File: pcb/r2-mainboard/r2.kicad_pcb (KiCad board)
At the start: 4 copper layers, 185.5 x 95 mm, 327 parts, among them J1 USB-C 16P, J2 Pico-Lock 504050-0391, J20 SWD+JTAG (DNP), J21 MICRO_SD(TFC-WPAPR-08), J22 HC-FPC-05-09-6RLTAG, J23 HC-FPC-05-09-6RLTAG, J24 HC-FPC-05-09-8RLTAG, J25 SolderPads 3x, J26 BTH-060-01-L-D-A-K-TR, J27 BTH-060-01-L-D-A-K-TR, J6 FPC-05F-50PH20, Q1 AO3401A, Q2 S8050, Q6 AO3400A, Q7 AO3401A, Q8 AO3401A, Q9 AO3400A, SW20 SW, SW21 SW, SW22 SW, U1 BQ25892RTW, U10 TPS7A0233DBVR, U12 TPS61022RWUR, U13 TPS63802DLAR, U14 TPS62A02DRLR, U15 TPS62A02DRLR, U2 MAX17048G+T10, U20 STM32G0B1RCT6, U21 INA3221, U22 INA3221, U23 LGS6302B5, U24 LGS6302B5, U26 LGS5145, U27 INA3221, U3 USBLC6-2SC6, U31 LM321, U41 XC6SLX-FTG256, U42 W25Q128JVSIQ, U52 MT41K64M16TW, U53 LM3630A, U54 TPS22914BYFPR, U55 TPS22914BYFPR, U6 MT9700, U7 TPS22914BYFPR, U8 TPS22914BYFPR, U9 LGS5145, X1 33.33MHz, X2 PCM-071, Y20 32.768kHz

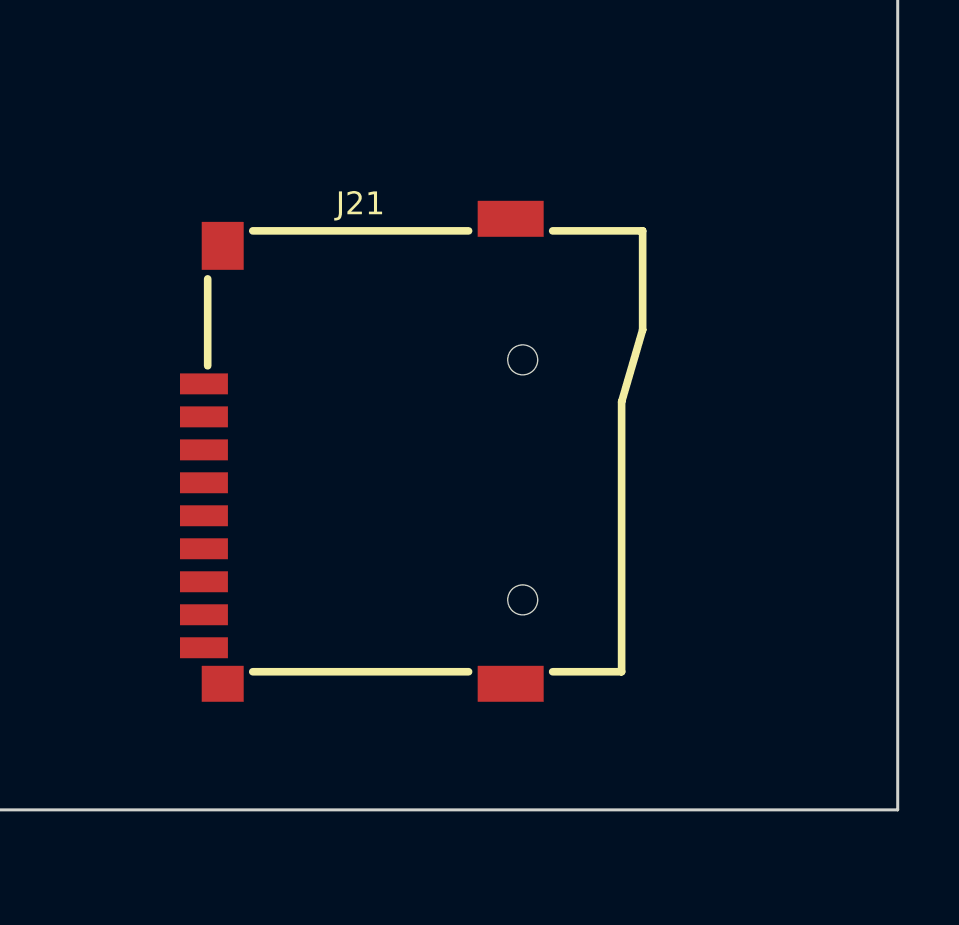
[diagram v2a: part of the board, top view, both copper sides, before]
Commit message: R2: 3D models — 322 of 327 now resolve, and the other five say why
After the path fix set KICAD10_3DMODEL_DIR, 311 of 327 footprints already
resolved. tools/add_3d_models.py handles the rest and makes the project
self-contained: everything it uses lands in 3dmodels/ referenced by
${KIPRJMOD}, so the 3D view works on any clone.

The assumption that R1 has these models is half right in a way worth
recording. pcb_common keeps 66 STEP files NEXT TO its footprints rather than
in a .3dshapes directory, which is why searching for 3D directories finds
nothing -- but several are referenced by absolute paths from the original
author, J24's pointing at /Users/wenting/Documents/projects/Enchanter/... .
Those are real models and are now copied in and re-pointed: J1's actual
HRO TYPE-C-31-M-12 (whose filename in pcb_common has a double space), J24,
J21's microSD socket and J6's panel connector. R1's own board is no better
off: 349 of its 378 model references point at files that do not exist.

The Spartan-6 is the other case entirely. footprints:Xilinx_FTG256 is a
pcb_common custom footprint whose model lived on the Modos author's KiCad 6
install -- hence ${KICAD6_3DMODEL_DIR}, a variable nothing defines any more
-- and KiCad's library has no Xilinx_FTG256 either. It now uses
BGA-256_17.0x17.0mm_Layout16x16_P1.0mm, which is the FTG256's exact
geometry. Six other parts get dimensional stand-ins, each recorded with what
matches and what does not.

Five are left with nothing, deliberately rather than faked: X1, L1, J2, U53
and J25 (which is bare copper pads and correctly has none). J2 is the one to
resist substituting -- only a 1.25 mm PicoBlade model exists, a different
connector, and it sits at the board edge where a wrong body would mislead
the enclosure check.

⚠ A stand-in is for clearance and collision, not identity. Body and height
are right; pin detail and markings are not.

One KiCad behaviour worth knowing: a footprint edited in the library does
not propagate to a board tha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
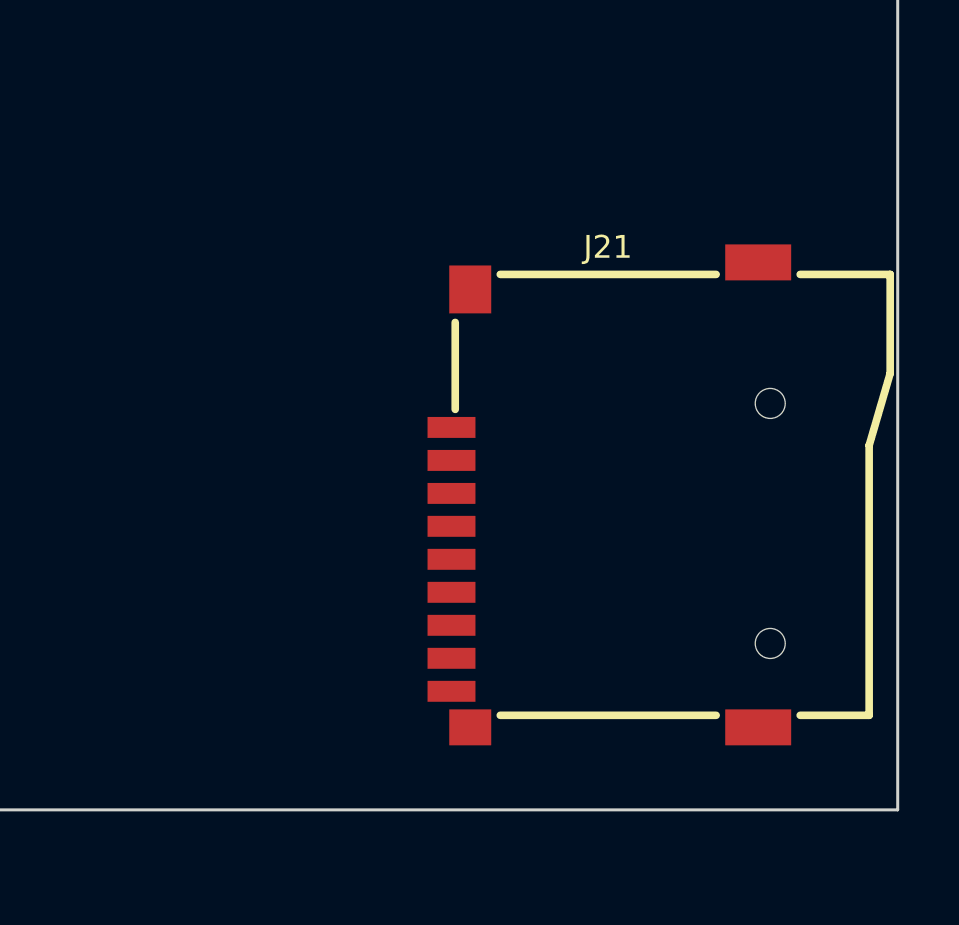
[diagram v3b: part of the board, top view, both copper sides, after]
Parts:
- moved J21 8.38 mm to (265.0, 103.0)
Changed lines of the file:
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@@
 		)
 		(embedded_fonts no)
+		(model "${KIPRJMOD}/3dmodels/BTH-060-01-L-D-A-K-TR.stp"
+			(offset (xyz 0 0 0))
+			(scale (xyz 1 1 1))
+			(rotate (xyz 0 0 0))
+		)
 	)
 	(footprint "Resistor_SMD:R_0402_1005Metric"
@@
 		)
 		(embedded_fonts no)
-		(model "${KICAD10_3DMODEL_DIR}/Connector_USB.3dshapes/USB_C_Receptacle_HRO_TYPE-C-31-M-12.step"
-			(offset
-				(xyz 0 0 0)
-			)
-			(scale
-				(xyz 1 1 1)
-			)
-			(rotate
-				(xyz 0 0 0)
-			)
+		(model "${KIPRJMOD}/3dmodels/HRO_TYPE-C-31-M-12.step"
+			(offset (xyz 0 0 0))
+			(scale (xyz 1 1 1))
+			(rotate (xyz 0 0 0))
 		)
 	)
@@
 		)
 		(embedded_fonts no)
-		(model "/Users/wenting/Documents/projects/Enchanter/pcb/pcb_common/footprints.pretty/FPC-SMD_8P-P0.50_HC-FPC-05-09-8RLTAG.step"
-			(offset
-				(xyz 0 0.65 0)
-			)
-			(scale
-				(xyz 1 1 1)
-			)
-			(rotate
-				(xyz 0 0 -180)
-			)
+		(model "${KIPRJMOD}/3dmodels/FPC-SMD_8P-P0.50_HC-FPC-05-09-8RLTAG.step"
+			(offset (xyz 0 0 0))
+			(scale (xyz 1 1 1))
+			(rotate (xyz 0 0 0))
 		)
 	)
 	(footprint "r2:PCM-071_Module"
 		(layer "F.Cu")
-		(attr exclude_from_pos_files allow_missing_courtyard)
 		(at 164.2 41.028 90)
 		(descr "PHYTEC phyCORE-AM62x PCM-071, module outline and M2.5 mounting holes. NO PADS -- the 240 contacts belong to J26/J27, the two BTH-060 receptacles. The module is fitted by hand after assembly, so this is excluded from the position file. Outline and hole positions from PCM-071_1573-1.dxf (BOARD_OUTLINE 32.000 x 43.000; holes at 2.800/2.800 and 29.200/40.200, 2.600 drill, 4.000 plating). Stands 5 mm off the board on two M2.5 F-F standoffs. See som.md section 11.")
@@
 			)
 		)
+		(attr exclude_from_pos_files allow_missing_courtyard)
 		(duplicate_pad_numbers_are_jumpers no)
 		(fp_line
@@
 		)
 		(fp_rect
-			(start -16 21.5)
-			(end 16 -21.5)
+			(start -14.1845 -19.9)
+			(end -8.2155 15.1)
 			(stroke
 				(width 0.1)
@@
 			)
 			(fill no)
-			(layer "F.Fab")
+			(layer "Dwgs.User")
 		)
-		(fp_circle
-			(center 13.2 -18.7)
-			(end 15.2 -18.7)
+		(fp_rect
+			(start 8.2155 -15.1)
+			(end 14.1845 19.9)
 			(stroke
 				(width 0.1)
-				(type dash)
+				(type solid)
 			)
 			(fill no)
-			(layer "F.Fab")
+			(layer "Dwgs.User")
 		)
-		(fp_circle
-			(center -13.2 18.7)
-			(end -11.2 18.7)
+		(fp_rect
+			(start -16 21.5)
+			(end 16 -21.5)
 			(stroke
 				(width 0.1)
-				(type dash)
+				(type solid)
 			)
 			(fill no)
-			(layer "F.Fab")
+			(layer "Dwgs.User")
 		)
 		(fp_rect
-			(start -14.1845 -19.9)
-			(end -8.2155 15.1)
+			(start -16 21.5)
+			(end 16 -21.5)
 			(stroke
 				(width 0.1)
@@
 			)
 			(fill no)
-			(layer "Dwgs.User")
+			(layer "F.Fab")
 		)
-		(fp_rect
-			(start 8.2155 -15.1)
-			(end 14.1845 19.9)
+		(fp_circle
+			(center 13.2 -18.7)
+			(end 15.2 -18.7)
 			(stroke
 				(width 0.1)
-				(type solid)
+				(type dash)
 			)
 			(fill no)
-			(layer "Dwgs.User")
+			(layer "F.Fab")
 		)
-		(fp_rect
-			(start -16 21.5)
-			(end 16 -21.5)
+		(fp_circle
+			(center -13.2 18.7)
+			(end -11.2 18.7)
 			(stroke
 				(width 0.1)
-				(type solid)
+				(type dash)
 			)
 			(fill no)
-			(layer "Dwgs.User")
+			(layer "F.Fab")
 		)
 		(pad "" np_thru_hole circle
@@
 		)
 		(embedded_fonts no)
+		(model "${KIPRJMOD}/3dmodels/PCM-071.step"
+			(offset (xyz 0 0 0))
+			(scale (xyz 1 1 1))
+			(rotate (xyz 0 0 0))
+		)
 	)
 	(footprint "Resistor_SMD:R_0402_1005Metric"
@@
 		)
 		(embedded_fonts no)
+		(model "${KICAD10_3DMODEL_DIR}/Package_DFN_QFN.3dshapes/DFN-10-1EP_2x3mm_P0.5mm_EP0.64x2.4mm.step"
+			(offset (xyz 0 0 0))
+			(scale (xyz 1 1 1))
+			(rotate (xyz 0 0 0))
+		)
 	)
 	(footprint "Resistor_SMD:R_0402_1005Metric"
@@
 		)
 		(embedded_fonts no)
-		(model "${KICAD10_3DMODEL_DIR}/Package_DFN_QFN.3dshapes/Texas_RGV0016A_VQFN-16-1EP_4x4mm_P0.65mm_EP2.1x2.1mm.step"
-			(offset
-				(xyz 0 0 0)
-			)
-			(scale
-				(xyz 1 1 1)
-			)
-			(rotate
-				(xyz 0 0 0)
-			)
+		(model "${KICAD10_3DMODEL_DIR}/Package_DFN_QFN.3dshapes/Texas_RSA_VQFN-16-1EP_4x4mm_P0.65mm_EP2.7x2.7mm.step"
+			(offset (xyz 0 0 0))
+			(scale (xyz 1 1 1))
+			(rotate (xyz 0 0 0))
 		)
 	)
@@
 		)
 		(embedded_fonts no)
-		(model "${KICAD10_3DMODEL_DIR}/Package_DFN_QFN.3dshapes/Texas_RWU0007A_VQFN-7_2x2mm_P0.5mm.step"
-			(offset
-				(xyz 0 0 0)
-			)
-			(scale
-				(xyz 1 1 1)
-			)
-			(rotate
-				(xyz 0 0 0)
-			)
+		(model "${KICAD10_3DMODEL_DIR}/Package_DFN_QFN.3dshapes/DFN-8-1EP_2x2mm_P0.5mm_EP0.6x1.2mm.step"
+			(offset (xyz 0 0 0))
+			(scale (xyz 1 1 1))
+			(rotate (xyz 0 0 0))
 		)
 	)
@@
 		)
 		(embedded_fonts no)
-		(model "${KICAD10_3DMODEL_DIR}/Package_DFN_QFN.3dshapes/Texas_RGV0016A_VQFN-16-1EP_4x4mm_P0.65mm_EP2.1x2.1mm.step"
-			(offset
-				(xyz 0 0 0)
-			)
-			(scale
-				(xyz 1 1 1)
-			)
-			(rotate
-				(xyz 0 0 0)
-			)
+		(model "${KICAD10_3DMODEL_DIR}/Package_DFN_QFN.3dshapes/Texas_RSA_VQFN-16-1EP_4x4mm_P0.65mm_EP2.7x2.7mm.step"
+			(offset (xyz 0 0 0))
+			(scale (xyz 1 1 1))
+			(rotate (xyz 0 0 0))
 		)
 	)
@@
 		)
 		(embedded_fonts no)
-		(model "${KIPRJMOD}/datasheets/SoM Phycore AM62x/BTH-060-01-L-D-A-K-TR/BTH-060-01-L-D-A-K-TR.stp"
-			(offset
-				(xyz 0 0 0)
-			)
-			(scale
-				(xyz 1 1 1)
-			)
-			(rotate
-				(xyz -90 -0 -90)
-			)
+		(model "${KIPRJMOD}/3dmodels/BTH-060-01-L-D-A-K-TR.stp"
+			(offset (xyz 0 0 0))
+			(scale (xyz 1 1 1))
+			(rotate (xyz 0 0 0))
 		)
 	)
@@
 		(model "${KICAD10_3DMODEL_DIR}/Connector_FFC-FPC.3dshapes/Hirose_FH12-8S-0.5SH_1x08-1MP_P0.50mm_Horizontal.step"
 			(offset
-				(xyz 0 0 0)
+				(xyz 0 -0.8 0)
 			)
 			(scale
-				(xyz 1 1 1)
+				(xyz 0.8 0.8 0.8)
 			)
 			(rotate
-				(xyz 0 0 0)
+				(xyz -0 -0 -90)
 			)
 		)
@@
 		)
 		(embedded_fonts no)
-		(model "${KICAD10_3DMODEL_DIR}/Package_DFN_QFN.3dshapes/Texas_RGV0016A_VQFN-16-1EP_4x4mm_P0.65mm_EP2.1x2.1mm.step"
-			(offset
-				(xyz 0 0 0)
-			)
-			(scale
-				(xyz 1 1 1)
-			)
-			(rotate
-				(xyz 0 0 0)
-			)
+		(model "${KICAD10_3DMODEL_DIR}/Package_DFN_QFN.3dshapes/Texas_RSA_VQFN-16-1EP_4x4mm_P0.65mm_EP2.7x2.7mm.step"
+			(offset (xyz 0 0 0))
+			(scale (xyz 1 1 1))
+			(rotate (xyz 0 0 0))
 		)
 	)
@@
 		)
 		(embedded_fonts no)
-		(model "${KIPRJMOD}/../pcb_common/footprints.pretty/FPC-SMD_50P-P0.50_FPC-05F-50PH20.step"
-			(offset
-				(xyz 0 1.6 0)
-			)
-			(scale
-				(xyz 1 1 1)
-			)
-			(rotate
-				(xyz 0 0 0)
-			)
+		(model "${KIPRJMOD}/3dmodels/FPC-SMD_50P-P0.50_FPC-05F-50PH20.step"
+			(offset (xyz 0 0 0))
+			(scale (xyz 1 1 1))
+			(rotate (xyz 0 0 0))
 		)
 	)
@@
 	(footprint "footprints:TFC-WPAPR-08"
 		(layer "F.Cu")
-		(at 256.7488 101.548)
+		(at 265 103)
 		(descr "OFFSET X-> -0.950MM")
 		(tags "OFFSET X-> -0.950MM")
@@
 		)
 		(embedded_fonts no)
-		(model "${KIPRJMOD}/../pcb_common/footprints.pretty/HY-TF1007B.STEP"
-			(offset
-				(xyz -7.25 -7.35 0)
-			)
-			(scale
-				(xyz 1 1 1)
-			)
-			(rotate
-				(xyz -90 0 -90)
-			)
+		(model "${KIPRJMOD}/3dmodels/HY-TF1007B.STEP"
+			(offset (xyz 0 0 0))
+			(scale (xyz 1 1 1))
+			(rotate (xyz 0 0 0))
 		)
 	)
@@
 		)
 		(embedded_fonts no)
-		(model "${KICAD10_3DMODEL_DIR}/Button_Switch_SMD.3dshapes/SW_Push_1P1T_XKB_TS-1187A.step"
-			(offset
-				(xyz 0 0 0)
-			)
-			(scale
-				(xyz 1 1 1)
-			)
-			(rotate
-				(xyz 0 0 0)
-			)
+		(model "${KICAD10_3DMODEL_DIR}/Button_Switch_SMD.3dshapes/SW_Push_1P1T_NO_CK_KMR2.step"
+			(offset (xyz 0 0 0))
+			(scale (xyz 1 1 1))
+			(rotate (xyz 0 0 0))
 		)
 	)
@@
 		)
 		(embedded_fonts no)
-		(model "${KICAD6_3DMODEL_DIR}/Package_BGA.3dshapes/Xilinx_FTG256.wrl"
-			(offset
-				(xyz 0 0 0)
-			)
-			(scale
-				(xyz 1 1 1)
-			)
-			(rotate
-				(xyz 0 0 0)
-			)
+		(model "${KICAD10_3DMODEL_DIR}/Package_BGA.3dshapes/BGA-256_17.0x17.0mm_Layout16x16_P1.0mm_Ball0.5mm_Pad0.4mm_NSMD.step"
+			(offset (xyz 0 0 0))
+			(scale (xyz 1 1 1))
+			(rotate (xyz 0 0 0))
 		)
 	)
@@
 		)
 		(embedded_fonts no)
-		(model "${KICAD10_3DMODEL_DIR}/Package_DFN_QFN.3dshapes/WQFN-24-1EP_4x4mm_P0.5mm_EP2.6x2.6mm.step"
-			(offset
-				(xyz 0 0 0)
-			)
-			(scale
-				(xyz 1 1 1)
-			)
-			(rotate
-				(xyz 0 0 0)
-			)
+		(model "${KICAD10_3DMODEL_DIR}/Package_DFN_QFN.3dshapes/Texas_RTW_WQFN-24-1EP_4x4mm_P0.5mm_EP2.7x2.7mm.step"
+			(offset (xyz 0 0 0))
+			(scale (xyz 1 1 1))
+			(rotate (xyz 0 0 0))
 		)
 	)
@@
 		)
 		(embedded_fonts no)
-		(model "${KICAD10_3DMODEL_DIR}/Package_DFN_QFN.3dshapes/TDFN-8-1EP_2x2mm_P0.5mm_EP0.8x1.2mm.step"
-			(offset
-				(xyz 0 0 0)
-			)
-			(scale
-				(xyz 1 1 1)
-			)
-			(rotate
-				(xyz 0 0 0)
-			)
+		(model "${KICAD10_3DMODEL_DIR}/Package_DFN_QFN.3dshapes/DFN-8-1EP_2x2mm_P0.5mm_EP0.6x1.2mm.step"
+			(offset (xyz 0 0 0))
+			(scale (xyz 1 1 1))
+			(rotate (xyz 0 0 0))
 		)
 	)
@@
 		(layer "Edge.Cuts")
 	)
-	(embedded_fonts no)
 	(group "SoM: X2 + J26 + J27"
-		(members
-			"2200e001-a954-48b2-9629-bd47b75f0930"
+		(members "1b24aa06-b18f-4e78-a7c5-cd93cf5dd40f" "2200e001-a954-48b2-9629-bd47b75f0930"
 			"81925fca-ef22-4cca-a487-e84efd632f81"
-			"1b24aa06-b18f-4e78-a7c5-cd93cf5dd40f"
 		)
 	)
+	(embedded_fonts no)
 )

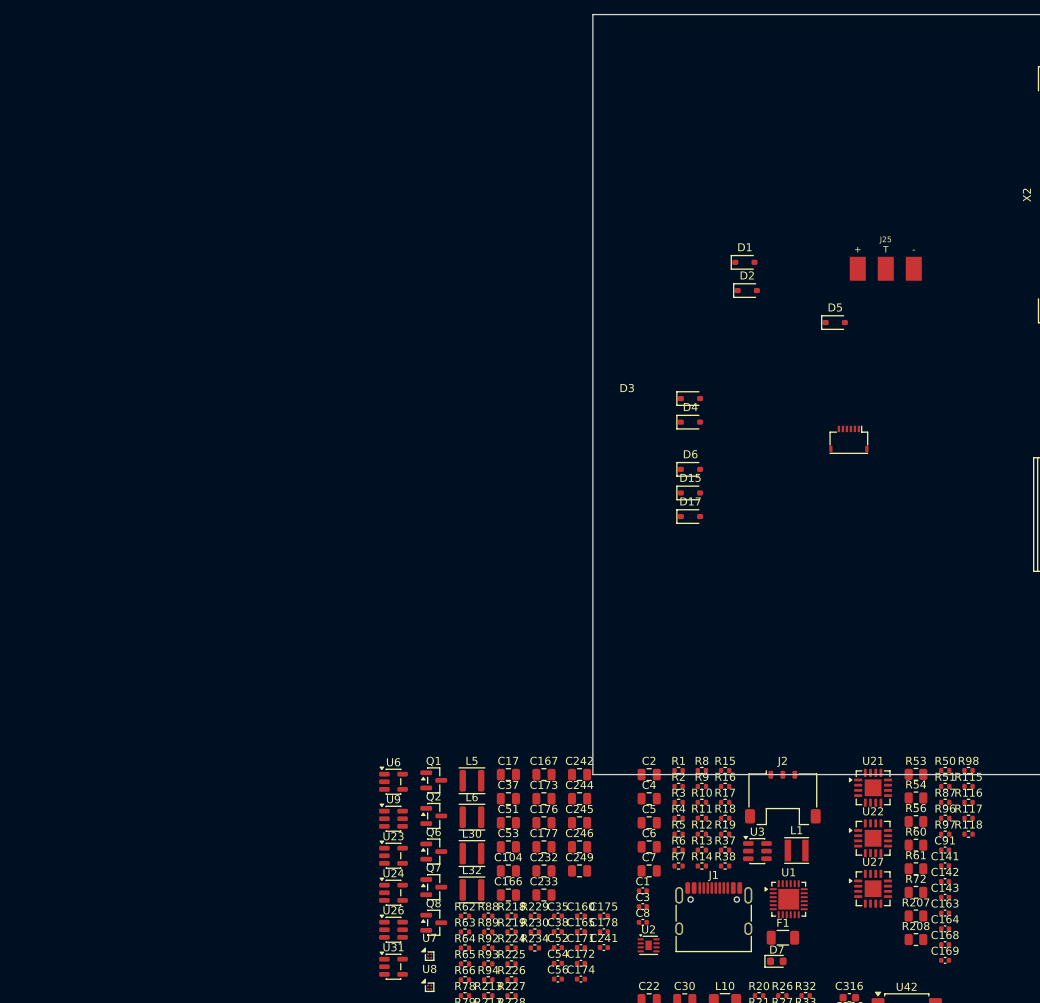
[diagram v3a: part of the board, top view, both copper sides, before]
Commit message: R2: import R1's design settings, and nine net classes with reasons attached
The owner is starting to route and asked what track widths to use. R2's
project file had never been through Board Setup: KiCad 10 stock values (0.4 mm
tracks, 1.651 mm vias) and one stray `power` class whose five patterns match
nets that do not exist on this board.

R2's stackup turns out to be byte-identical to R1's -- same 0.127 mm prepreg,
0.6 mm core, 0.035 mm outer copper, ENIG -- so every geometry R1 proved at
DDR3-666 on a Spartan-6 transfers with its impedance intact. That is the whole
justification for copying rather than calculating, and it is why R1's
SDRAM/EPD/USB widths come across verbatim.

tools/import_r1_settings.py does it in one gated step. It reads R1 read-only,
refuses to write while KiCad is open (KiCad rewrites the project from memory on
save, so the edit would vanish with no error), backs up, and prints every
change plus the reason for each class.

Three things are deliberately not R1's:

- Clearance. layout.md §6.1 used to say start at 0.2 mm. Measuring the placed
  footprints shows that is unusable: KiCad checks class clearance pad-to-pad
  INSIDE a footprint, and U1's BQ25792 has 0.125 mm between pads 1 and 24 --
  0.2 mm would flag eight packages on the day of import. R1's 0.11 mm clears
  every one. §6.1 corrected, the measurements recorded in a new §4.2.

- HV clearance is 0.11 like everything else, and the real separation lives in a
  new r2.kicad_dru rule restricted to tracks. +VGH lands on a 0.5 mm-pitch
  VSON-HR-10 whose own pads sit 0.25 mm apart, so a wide class clearance would
  produce DRC errors no routing can clear.

- An eighth class, EPD, for the 23 EPDC_* nets. layout.md §4's table listed
  seven and was silent on them -- the second-largest routed group on the board.
  R1 had a class for them; without it they would have routed on Default.

check_pcb.py's net-class check was reading the wrong file: it grepped
r2.kicad_pcb for `(net_class "..."` and 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
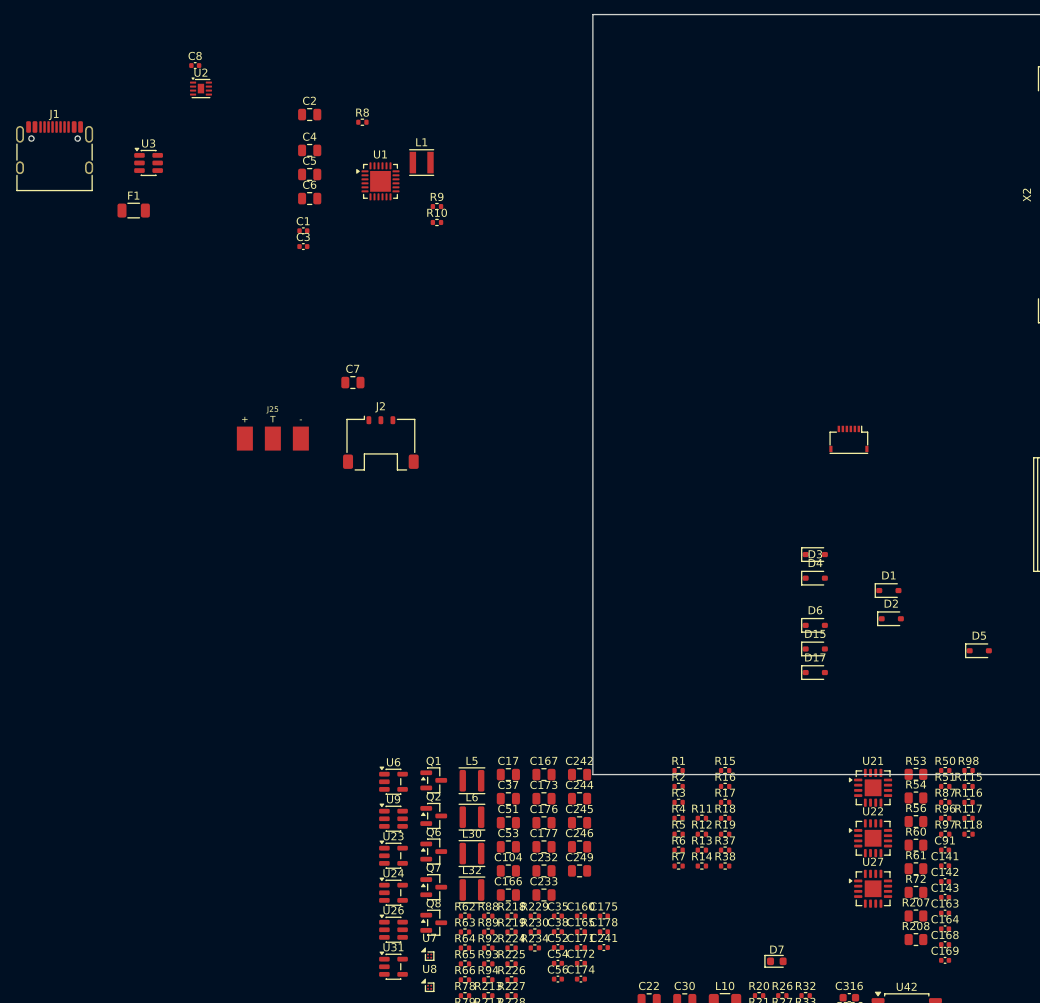
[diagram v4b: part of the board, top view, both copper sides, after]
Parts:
- moved J1 125.8 mm to (19.7, 36.6)
- moved F1 121.9 mm to (29.6, 43.0)
- moved C8 120.8 mm to (37.3, 24.9)
- moved U2 120.8 mm to (38.0, 27.8)
- moved U3 114.9 mm to (31.5, 37.0)
- moved U1 103.2 mm to (60.5, 39.4)
- moved L1 97.9 mm to (65.6, 37.0)
- moved C1 92.8 mm to (50.8, 45.5)
- moved C2 92.8 mm to (51.6, 31.0)
- moved C3 92.8 mm to (50.8, 47.5)
- moved R8 91.5 mm to (58.2, 32.0)
- moved C4 91.5 mm to (51.6, 35.5)
- moved C5 91.5 mm to (51.6, 38.5)
- moved C6 91.5 mm to (51.6, 41.5)
- moved R9 79.7 mm to (67.5, 42.5)
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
